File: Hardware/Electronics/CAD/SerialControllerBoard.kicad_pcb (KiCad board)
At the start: 2 copper layers, 45 x 60 mm, 32 parts, among them J1 Conn_01x02, J10 Conn_01x04, J11 Conn_01x04, J2 Conn_01x03, J3 Conn_01x03, J4 Conn_01x03, J5 Conn_01x03, J6 Conn_01x02, J7 Conn_01x02, J8 Conn_02x03_Odd_Even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

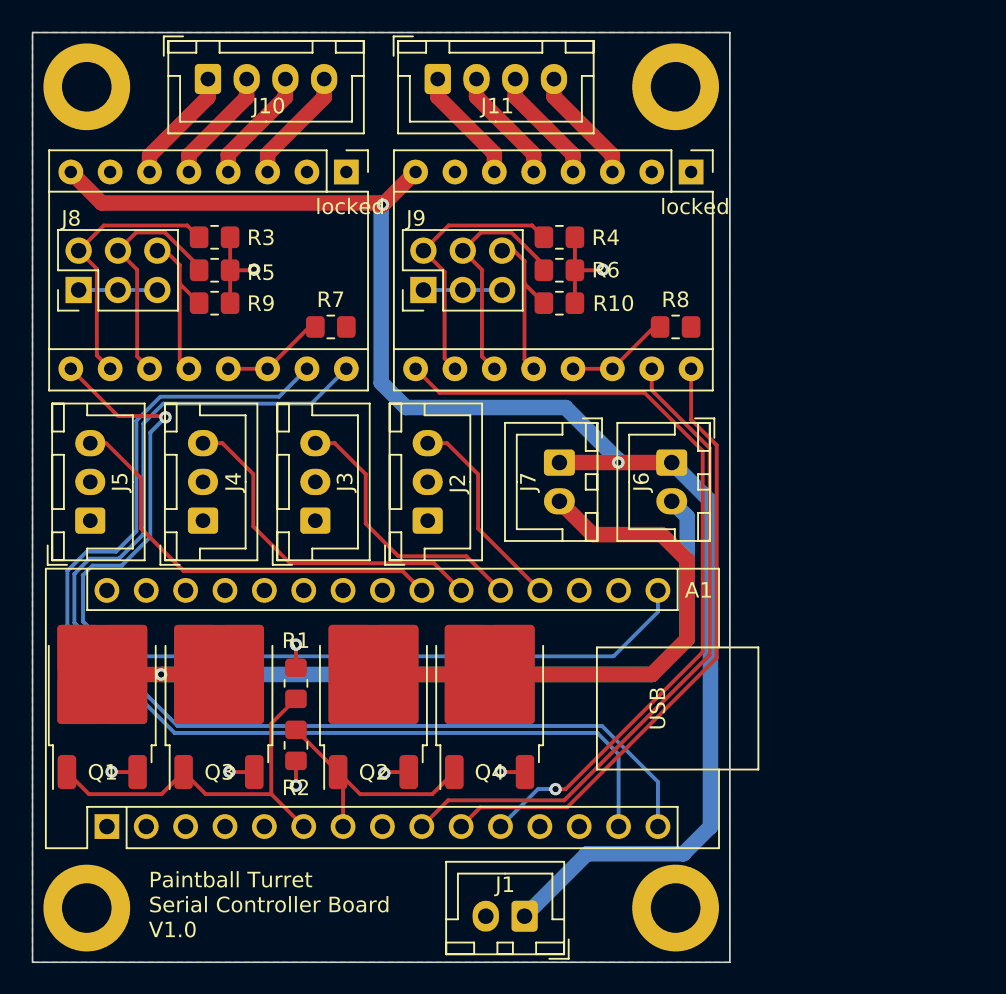
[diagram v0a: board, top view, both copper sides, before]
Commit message: New controller board Layout with USB Hub and Arduino SoM
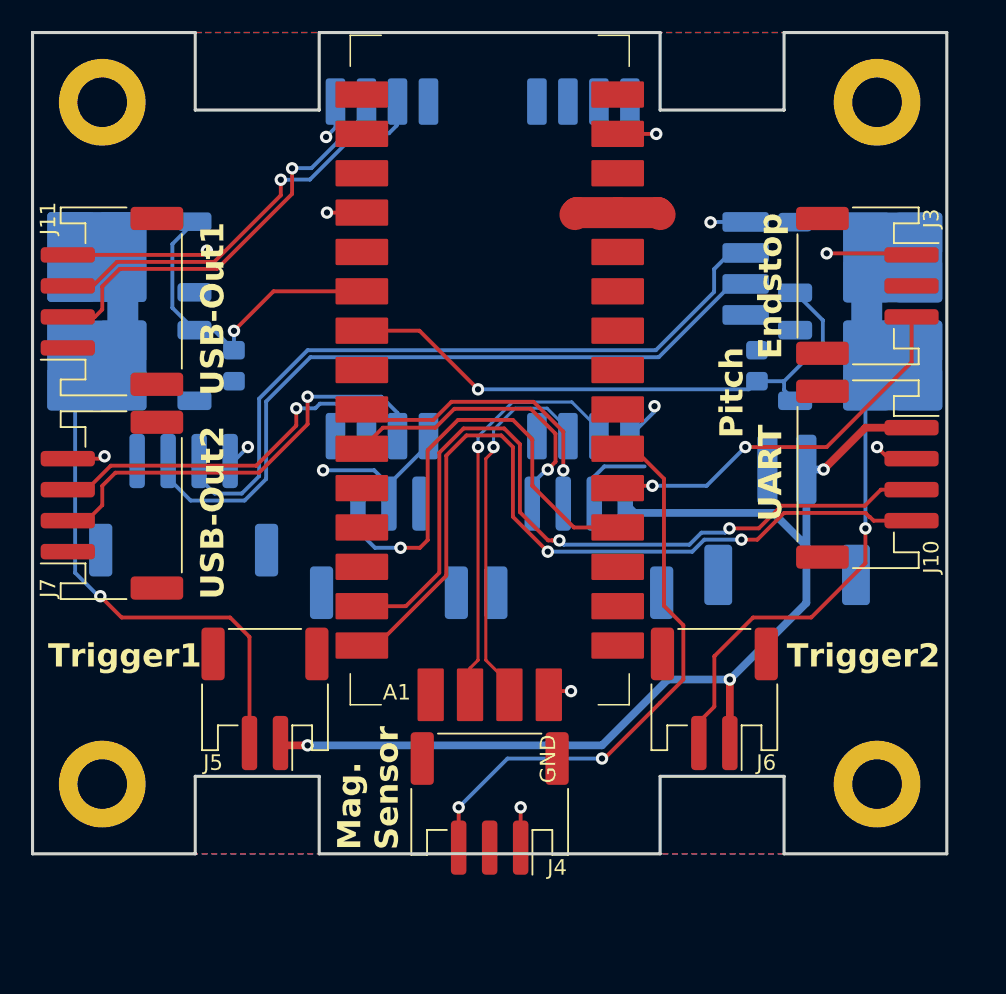
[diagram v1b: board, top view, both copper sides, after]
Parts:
- removed the J4 at (131.0, 71.5)
- removed R10, R3, R4, R5, R6, R7, R8, R9: 10k, Resistor_SMD:R_0805_2012Metric_Pad1.20x1.40mm_HandSolder
- removed locked (x2): Pololu_Breakout_A4988, Module:Pololu_Breakout-16_15.2x20.3mm
- added J7: Conn_01x04, Connector_JST:JST_PH_S4B-PH-SM4-TB_1x04-1MP_P2.00mm_Horizontal, F.Cu at (125.1, 70.5)
- added U1: FE11SX4, FE11SX4:FE11SX4, B.Cu at (150.2, 55.2)
- A1: footprint Module:Arduino_Nano -> Module:Arduino_Nano_SoM
- J1: footprint Connector_JST:JST_XH_B2B-XH-A_1x02_P2.50mm_Vertical -> JST-XH-Addon:JST_XH_S2B-XH-SM4-TB_1x02-1MP_P2.50mm_Horizontal; moved to B.Cu
- J10, J11: footprint Connector_JST:JST_XH_B4B-XH-A_1x04_P2.50mm_Vertical -> Connector_JST:JST_PH_S4B-PH-SM4-TB_1x04-1MP_P2.00mm_Horizontal
- J2: footprint Connector_JST:JST_XH_B3B-XH-A_1x03_P2.50mm_Vertical -> Connector_JST:JST_PH_S3B-PH-SM4-TB_1x03-1MP_P2.00mm_Horizontal; moved to B.Cu
- J3: footprint Connector_JST:JST_XH_B3B-XH-A_1x03_P2.50mm_Vertical -> Connector_JST:JST_PH_S3B-PH-SM4-TB_1x03-1MP_P2.00mm_Horizontal
- J4: renamed from J5; footprint Connector_JST:JST_XH_B3B-XH-A_1x03_P2.50mm_Vertical -> Connector_JST:JST_PH_S3B-PH-SM4-TB_1x03-1MP_P2.00mm_Horizontal
- J5: renamed from J6; footprint Connector_JST:JST_XH_B2B-XH-A_1x02_P2.50mm_Vertical -> Connector_JST:JST_PH_S2B-PH-SM4-TB_1x02-1MP_P2.00mm_Horizontal
- J6: renamed from J7; footprint Connector_JST:JST_XH_B2B-XH-A_1x02_P2.50mm_Vertical -> Connector_JST:JST_PH_S2B-PH-SM4-TB_1x02-1MP_P2.00mm_Horizontal
- J8, J9: value Conn_02x03_Odd_Even -> Conn_01x04; footprint Connector_PinHeader_2.54mm:PinHeader_2x03_P2.54mm_Vertical -> Connector_JST:JST_PH_S4B-PH-SM4-TB_1x04-1MP_P2.00mm_Horizontal; moved to B.Cu
- Q1, Q2, Q3, Q4, R1, R2: moved to B.Cu
- moved J10 49.6 mm to (173.9, 68.5), turned to -90 degrees
- moved J3 38.7 mm to (173.9, 56.4), turned to -90 degrees
- moved Q2 38.6 mm to (174.2, 61.5), turned to 0 degrees
- moved R2 38.5 mm to (166.8, 61.5), turned to 90 degrees
- moved Q4 37.5 mm to (174.2, 54.5), turned to 0 degrees
- moved J4 31.6 mm to (149.5, 89.8), turned to 180 degrees
- moved J1 30.7 mm to (168.7, 71.5)
- moved J5 30.4 mm to (135.0, 83.0), turned to 180 degrees
- moved Q1 28.2 mm to (125.4, 54.5), turned to 180 degrees
- moved J11 25.5 mm to (125.1, 57.3), turned to 90 degrees
- moved Q3 22.2 mm to (125.4, 61.5), turned to 180 degrees
- moved R1 20.9 mm to (133.0, 61.5), turned to -90 degrees
- moved A1 20.2 mm to (141.2, 79.6)
- moved J9 19.4 mm to (155.2, 73.2), turned to 180 degrees
- moved J6 18.2 mm to (164.0, 83.0), turned to 180 degrees
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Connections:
- net endstop-pitch-1 renamed endstop-pitch
- A1 pad 10: pitch-dir -> yaw-uart-tx
- A1 pad 11: pitch-enable -> unconnected-(A1-D8-Pad11)
- A1 pad 14: yaw-step -> pitch-uart-rx
- A1 pad 15: yaw-dir -> pitch-uart-tx
- A1 pad 16: yaw-enable -> unconnected-(A1-D13-Pad16)
- A1 pad 21: endstop-pitch-2 -> mag-sensor
- A1 pad 22: mag-sensor -> unconnected-(A1-A3-Pad22)
- A1 pad 9: pitch-step -> yaw-uart-rx
- J10 pad 1: Net-(A2-2B) -> VCC
- J10 pad 2: Net-(A2-2A) -> GND
- J10 pad 3: Net-(A2-1A) -> pitch-uart-rx
- J10 pad 4: Net-(A2-1B) -> pitch-uart-tx
- J11 pad 1: Net-(A3-2B) -> +5V
- J11 pad 4: Net-(A3-1B) -> GND
- J8 pad 3: +5V -> Net-(J8-Pin_3)
- J8 pad 4: Net-(A2-MS2) -> GND
- J9 pad 1: +5V -> VCC
- J9 pad 2: Net-(A3-MS1) -> GND
- J9 pad 3: +5V -> yaw-uart-rx
- J9 pad 4: Net-(A3-MS2) -> yaw-uart-tx
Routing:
- net yaw-dir: track 75.2 -> 0.00 mm
- net yaw-step: track 72.2 -> 0.00 mm
- net yaw-enable: track 64.5 -> 0.00 mm, vias 1 -> 0
- net pitch-uart-tx: track 0.00 -> 52.6 mm, vias 0 -> 2
- net pitch-uart-rx: track 0.00 -> 51.9 mm, vias 0 -> 2
- net pitch-enable: track 51.4 -> 0.00 mm, vias 1 -> 0
- net Net-(J8-Pin_3): track 0.00 -> 47.7 mm
- net pitch-step: track 43.2 -> 0.00 mm
- net pitch-dir: track 40.3 -> 0.00 mm
- net Net-(J8-Pin_2): track 17.2 -> 47.0 mm
- net Net-(J7-Pin_2): track 0.00 -> 28.3 mm, vias 0 -> 1
- net VCC: track 99.2 -> 71.2 mm, vias 2 -> 3
- net USB-D-: track 0.00 -> 27.2 mm, vias 0 -> 1
- net USB-D+: track 0.00 -> 24.3 mm, vias 0 -> 1
- net Net-(J7-Pin_3): track 0.00 -> 24.0 mm, vias 0 -> 1
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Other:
- board size 45 x 60 mm -> 59 x 53 mm
- board text added: "Endstop"
- board text added: "Mag. Sensor"
- board text added: "Paintball Turret Serial Controller Board V2.0"
- board text added: "Pitch"
- board text added: "Power"
- board text added: "Trigger1"
- board text added: "Trigger2"
- board text added: "UART"
- board text added: "USB-In"
- board text added: "USB-Out1"
- board text added: "USB-Out2"
- board text added: "Yaw"
- board text removed: "Paintball Turret Serial Controller Board V1.0"
